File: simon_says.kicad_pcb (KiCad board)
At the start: 2 copper layers, 97 x 60 mm, 19 parts, among them SW1 SW_Push_LED, SW2 SW_Push_LED, SW3 SW_Push_LED, SW4 SW_Push_LED, U1 ATtiny25-20P

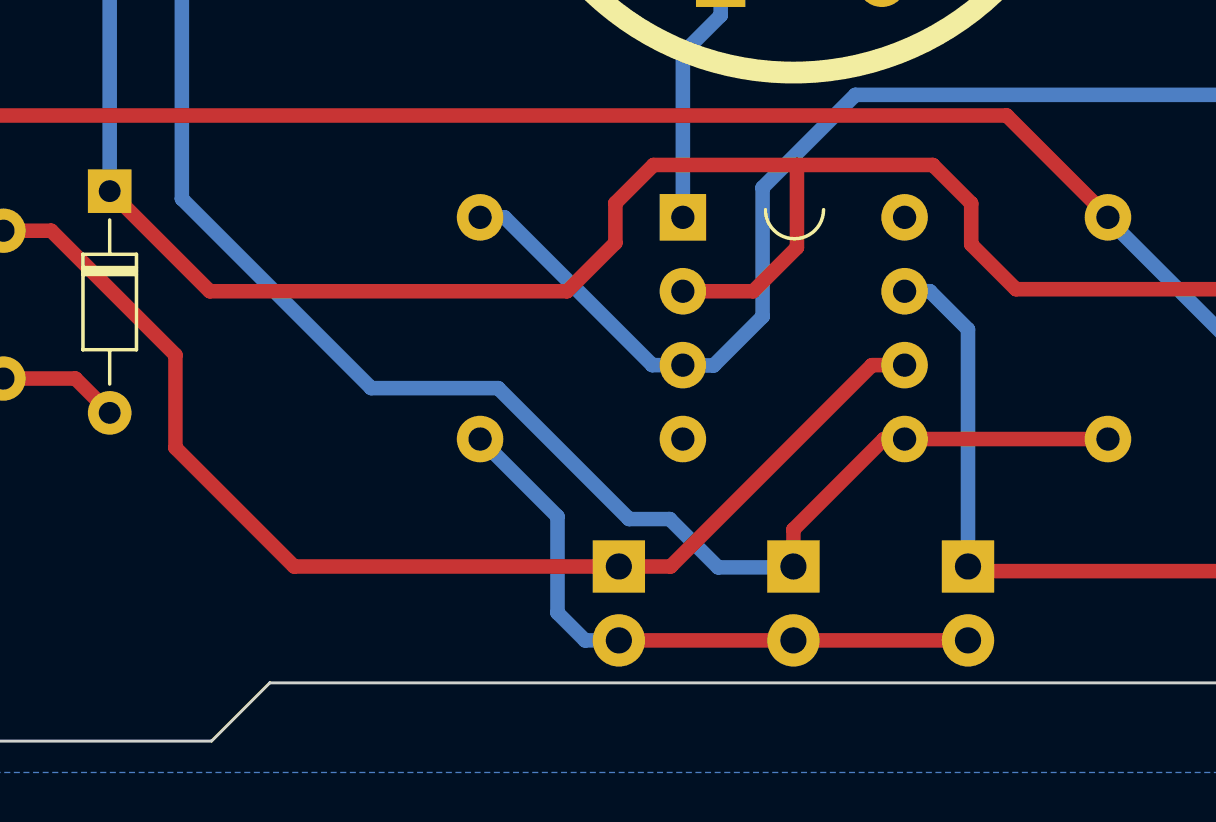
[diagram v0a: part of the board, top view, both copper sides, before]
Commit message: Added pads for power
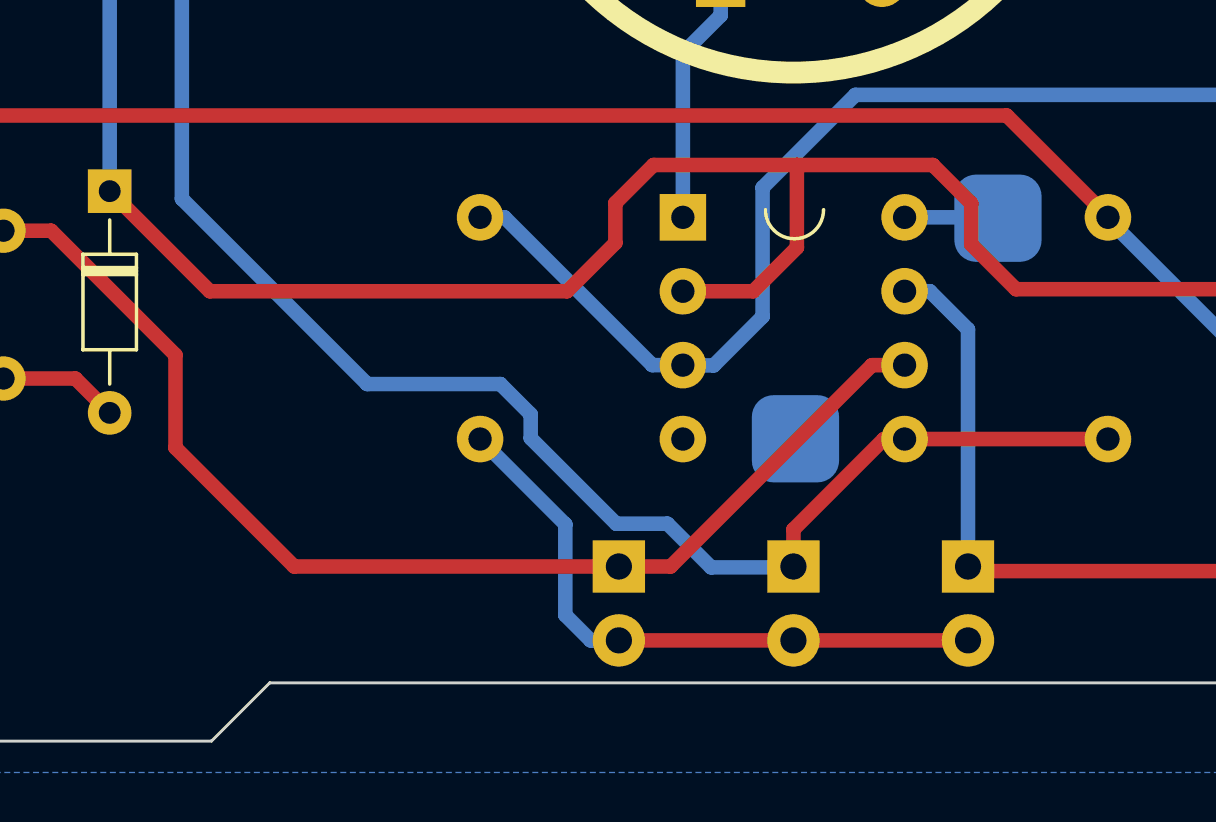
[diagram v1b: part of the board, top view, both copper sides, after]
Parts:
- added REF**: SolderWirePad_1x01_SMD_1x2mm, Connector_Wire:SolderWirePad_1x01_SMD_1x2mm, B.Cu at (98.6, 149.6)
- added REF**: SolderWirePad_1x01_SMD_1x2mm, Connector_Wire:SolderWirePad_1x01_SMD_1x2mm, B.Cu at (105.5, 142.0)
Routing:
- net +BATT: track 0.00 -> 3.44 mm
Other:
- board text added: "+"
- board text added: "-"
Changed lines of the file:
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@@
     (pad "1" thru_hole circle locked (at 0 0) (size 4.7 4.7) (drill 2.7) (layers "*.Cu" "*.Mask"))
   )
+  (footprint "Connector_Wire:SolderWirePad_1x01_SMD_1x2mm" (layer "B.Cu")
+    (at 98.57 149.61 180)
+    (descr "Wire Pad, Square, SMD Pad,  1mm x 2mm,")
+    (tags "MesurementPoint Square SMDPad 1mmx2mm ")
+    (attr exclude_from_pos_files exclude_from_bom)
+    (fp_text reference "REF**" (at 0 2.54) (layer "B.SilkS") hide
+        (effects (font (size 1 1) (thickness 0.15)) (justify mirror))
+    )
+    (fp_text value "SolderWirePad_1x01_SMD_1x2mm" (at 0 -2.54) (layer "B.Fab") hide
+        (effects (font (size 1 1) (thickness 0.15)) (justify mirror))
+    )
+    (pad "1" smd roundrect (at 0 0 180) (size 3 3) (layers "B.Cu" "B.Paste" "B.Mask") (roundrect_rratio 0.25)
+      (net 13 "-BATT"))
+  )
+  (footprint "Connector_Wire:SolderWirePad_1x01_SMD_1x2mm" (layer "B.Cu")
+    (at 105.53 142.03 180)
+    (descr "Wire Pad, Square, SMD Pad,  1mm x 2mm,")
+    (tags "MesurementPoint Square SMDPad 1mmx2mm ")
+    (attr exclude_from_pos_files exclude_from_bom)
+    (fp_text reference "REF**" (at 0 2.54) (layer "B.SilkS") hide
+        (effects (font (size 1 1) (thickness 0.15)) (justify mirror))
+    )
+    (fp_text value "SolderWirePad_1x01_SMD_1x2mm" (at 0 -2.54) (layer "B.Fab") hide
+        (effects (font (size 1 1) (thickness 0.15)) (justify mirror))
+    )
+    (pad "1" smd roundrect (at 0 0 180) (size 3 3) (layers "B.Cu" "B.Paste" "B.Mask") (roundrect_rratio 0.25)
+      (net 14 "+BATT"))
+  )
   (gr_line (start 115 103) (end 115 115.5)
     (stroke (width 0.32) (type default)) (layer "F.Cu"))
@@
     )
   )
+  (gr_text "+" (at 105.57 138.86) (layer "B.SilkS")
+    (effects (font (size 2 2) (thickness 0.3) bold) (justify mirror))
+  )
+  (gr_text "-" (at 99.63 147.7) (layer "B.SilkS")
+    (effects (font (size 1.5 1.5) (thickness 0.3) bold) (justify left bottom mirror))
+  )
   (segment (start 98.62 140.2) (end 103.29 140.2) (width 0.5) (layer "F.Cu") (net 1))
   (segment (start 104.61 141.52) (end 104.61 142.93) (width 0.5) (layer "F.Cu") (net 1))
@@
   (segment (start 102.32 149.62) (end 101.61 149.62) (width 0.5) (layer "F.Cu") (net 7))
   (segment (start 101.61 149.62) (end 98.5 152.73) (width 0.5) (layer "F.Cu") (net 7))
-  (segment (start 77.48 141.36) (end 83.99 147.87) (width 0.5) (layer "B.Cu") (net 7))
-  (segment (start 92.85 152.37) (end 94.25 152.37) (width 0.5) (layer "B.Cu") (net 7))
-  (segment (start 88.35 147.87) (end 92.85 152.37) (width 0.5) (layer "B.Cu") (net 7))
+  (segment (start 92.41 152.53) (end 94.17 152.53) (width 0.5) (layer "B.Cu") (net 7))
+  (segment (start 95.67 154.03) (end 98.47 154.03) (width 0.5) (layer "B.Cu") (net 7))
+  (segment (start 77.48 117.51) (end 77.48 141.36) (width 0.5) (layer "B.Cu") (net 7))
+  (segment (start 88.43 147.73) (end 89.47 148.77) (width 0.5) (layer "B.Cu") (net 7))
+  (segment (start 83.85 147.73) (end 88.43 147.73) (width 0.5) (layer "B.Cu") (net 7))
   (segment (start 72.63 116.27) (end 76.24 116.27) (width 0.5) (layer "B.Cu") (net 7))
   (segment (start 76.24 116.27) (end 77.48 117.51) (width 0.5) (layer "B.Cu") (net 7))
-  (segment (start 94.25 152.37) (end 95.91 154.03) (width 0.5) (layer "B.Cu") (net 7))
-  (segment (start 95.91 154.03) (end 98.47 154.03) (width 0.5) (layer "B.Cu") (net 7))
-  (segment (start 98.47 154.03) (end 98.5 154) (width 0.5) (layer "B.Cu") (net 7))
   (segment (start 71.35 117.54) (end 71.36 117.54) (width 0.5) (layer "B.Cu") (net 7))
-  (segment (start 77.48 117.51) (end 77.48 141.36) (width 0.5) (layer "B.Cu") (net 7))
+  (segment (start 89.47 149.59) (end 92.41 152.53) (width 0.5) (layer "B.Cu") (net 7))
   (segment (start 71.36 117.54) (end 72.63 116.27) (width 0.5) (layer "B.Cu") (net 7))
-  (segment (start 83.99 147.87) (end 88.35 147.87) (width 0.5) (layer "B.Cu") (net 7))
+  (segment (start 89.47 148.77) (end 89.47 149.59) (width 0.5) (layer "B.Cu") (net 7))
+  (segment (start 77.48 141.36) (end 83.85 147.73) (width 0.5) (layer "B.Cu") (net 7))
+  (segment (start 94.17 152.53) (end 95.67 154.03) (width 0.5) (layer "B.Cu") (net 7))
+  (segment (start 98.47 154.03) (end 98.5 154) (width 0.5) (layer "B.Cu") (net 7))
   (segment (start 104.34 156.54) (end 104.5 156.7) (width 0.5) (layer "F.Cu") (net 8))
   (segment (start 92.5 156.54) (end 104.34 156.54) (width 0.5) (layer "F.Cu") (net 8))
-  (segment (start 90.39 152.28) (end 90.39 155.59) (width 0.5) (layer "B.Cu") (net 8))
-  (segment (start 87.73 149.62) (end 90.39 152.28) (width 0.5) (layer "B.Cu") (net 8))
-  (segment (start 91.34 156.54) (end 92.5 156.54) (width 0.5) (layer "B.Cu") (net 8))
-  (segment (start 90.39 155.59) (end 91.34 156.54) (width 0.5) (layer "B.Cu") (net 8))
+  (segment (start 87.73 149.62) (end 90.66 152.55) (width 0.5) (layer "B.Cu") (net 8))
+  (segment (start 90.66 155.67) (end 91.53 156.54) (width 0.5) (layer "B.Cu") (net 8))
+  (segment (start 90.66 152.55) (end 90.66 155.67) (width 0.5) (layer "B.Cu") (net 8))
+  (segment (start 91.53 156.54) (end 92.5 156.54) (width 0.5) (layer "B.Cu") (net 8))
   (segment (start 94.28 154) (end 81.34 154) (width 0.5) (layer "F.Cu") (net 9))
   (segment (start 77.26 146.73) (end 72.99 142.46) (width 0.5) (layer "F.Cu") (net 9))
@@
   (segment (start 96 133.92) (end 96 135.06) (width 0.5) (layer "B.Cu") (net 12))
   (segment (start 96 135.06) (end 94.7 136.36) (width 0.5) (layer "B.Cu") (net 12))
+  (segment (start 102.32 142) (end 105.58 142) (width 0.5) (layer "B.Cu") (net 14))
+  (segment (start 105.58 142) (end 105.71 141.87) (width 0.25) (layer "B.Cu") (net 14))
   (zone (net 13) (net_name "-BATT") (layer "B.Cu") (hatch edge 0.5)
     (connect_pads (clearance 0.5))

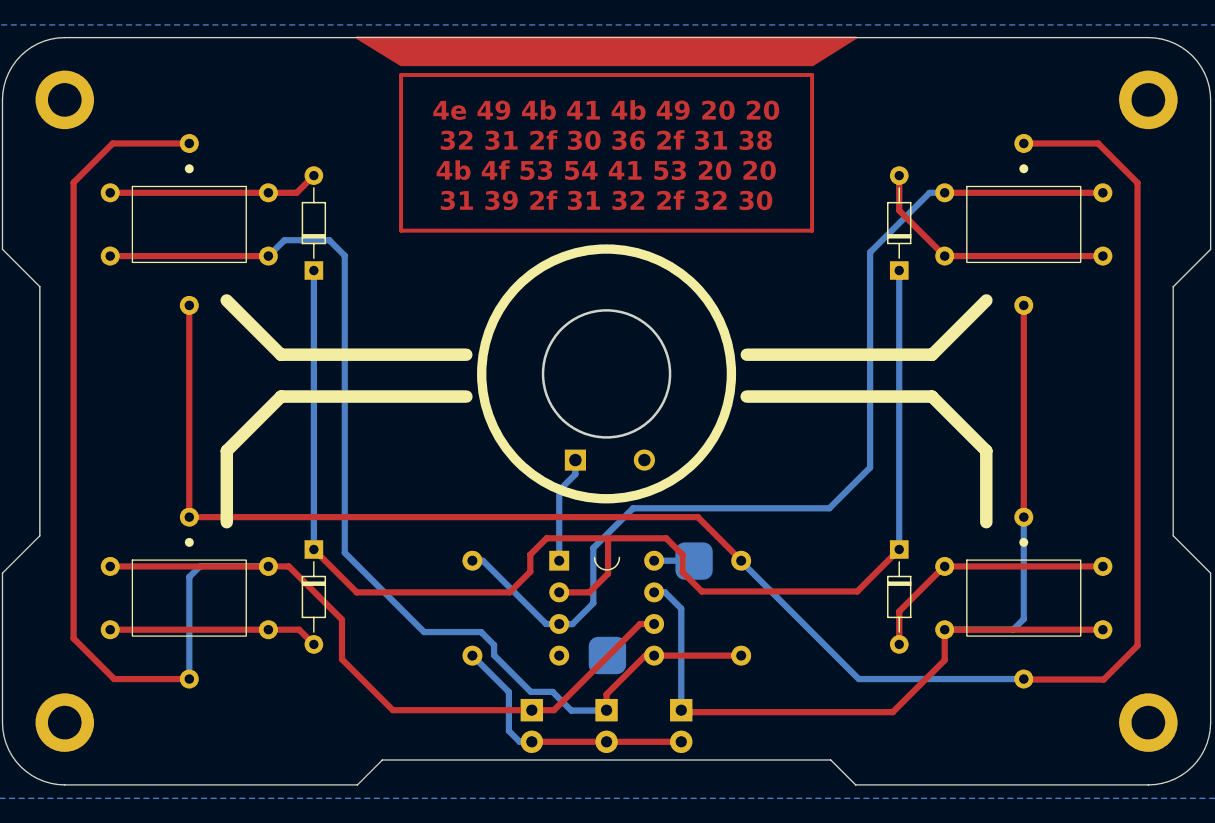
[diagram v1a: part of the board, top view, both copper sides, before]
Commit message: Added CR battery pads and removed redundant LEDs
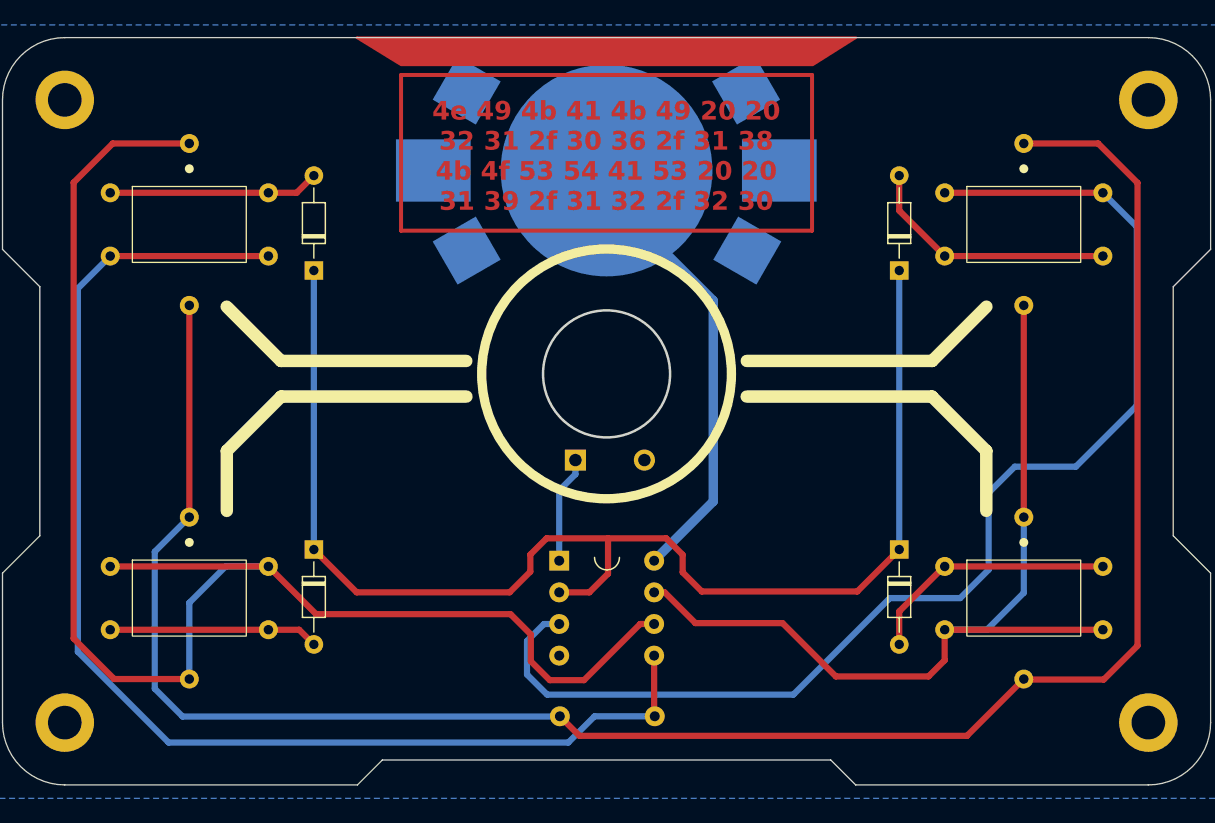
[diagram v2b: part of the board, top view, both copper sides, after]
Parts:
- removed D10, D6, D8: LED, LED_THT:LED_D1.8mm_W3.3mm_H2.4mm
- removed R2: 50R, Resistor_THT:R_Axial_DIN0207_L6.3mm_D2.5mm_P7.62mm_Horizontal
- added ?: , , F.Cu at (88.8, 104.3)
- added ?: , , F.Cu at (87.4, 117.1)
- added ?: , , F.Cu at (85.6, 110.7)
- added ?: , , F.Cu at (111.4, 104.3)
- added REF**: SolderWirePad_1x01_SMD_1x2mm, Connector_Wire:SolderWirePad_1x01_SMD_1x2mm, B.Cu at (109.7, 117.1)
- moved REF** 41.1 mm to (111.9, 110.7), turned to -90 degrees
- moved REF** 32.1 mm to (98.5, 110.7)
- moved R1 8.48 mm to (102.4, 154.5), turned to 180 degrees
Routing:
- net +BATT: track 3.44 -> 36.8 mm
- net Net-(D10-A): track 21.5 -> 0.00 mm
- net MM4: track 79.9 -> 99.7 mm
- net MM1: track 83.8 -> 100.7 mm
- net Net-(SW1-A): track 147.3 -> 163.1 mm
- net MM3: track 80.9 -> 72.5 mm
- net MM2: track 125.9 -> 122.1 mm
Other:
- board text added: "CR2450"
- board text removed: "+"
- board text removed: "-"

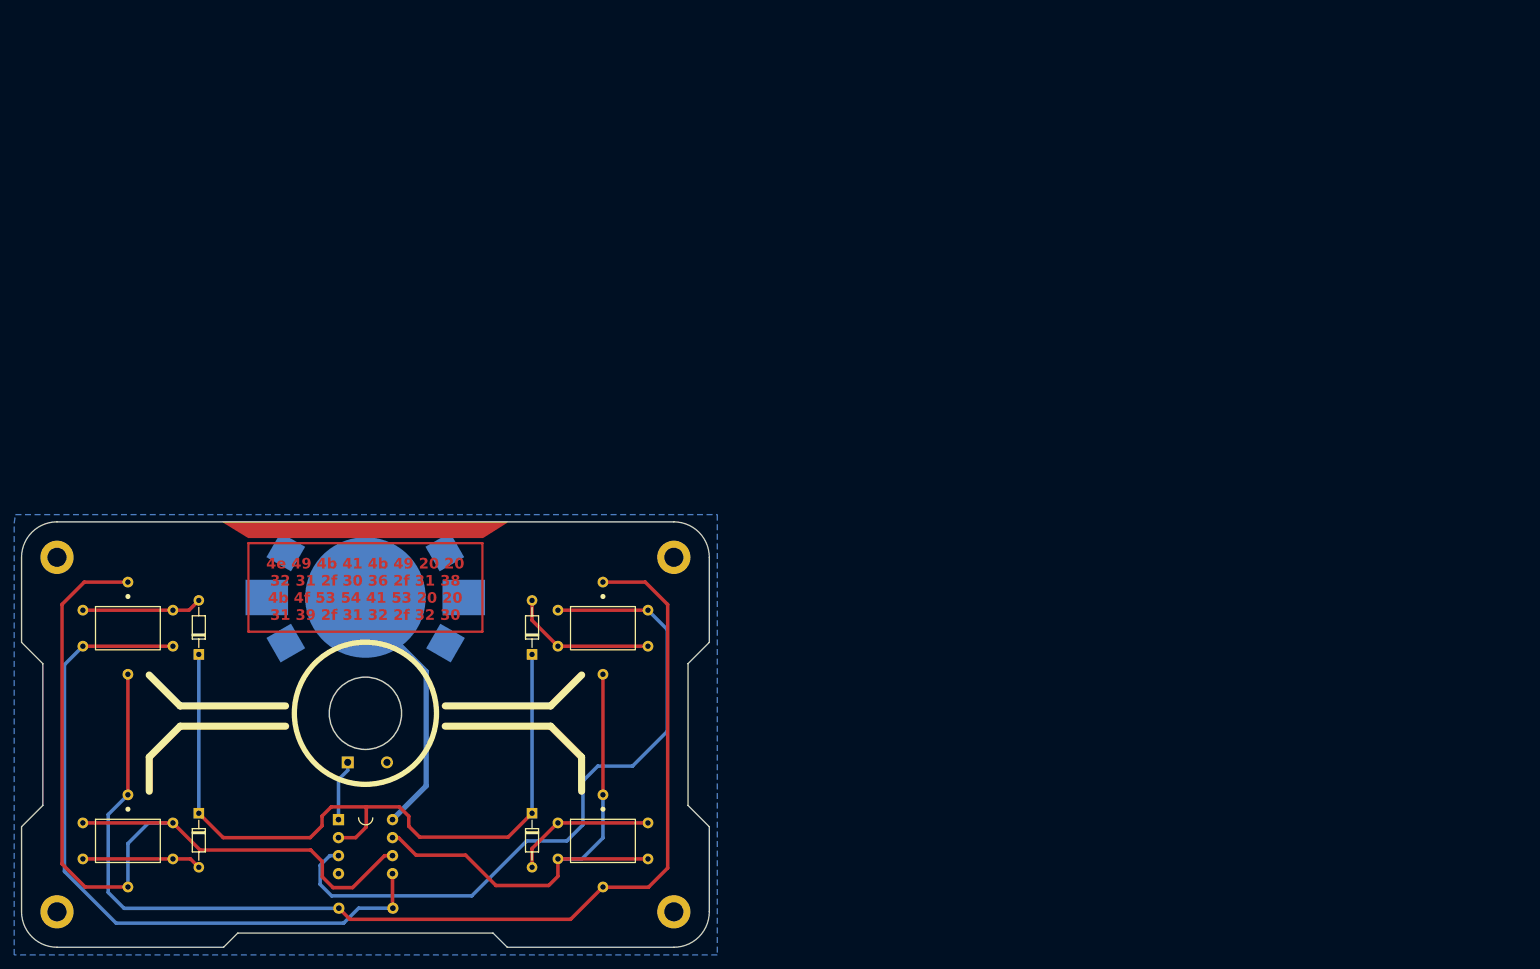
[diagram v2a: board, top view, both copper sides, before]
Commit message: Updated front face decorations
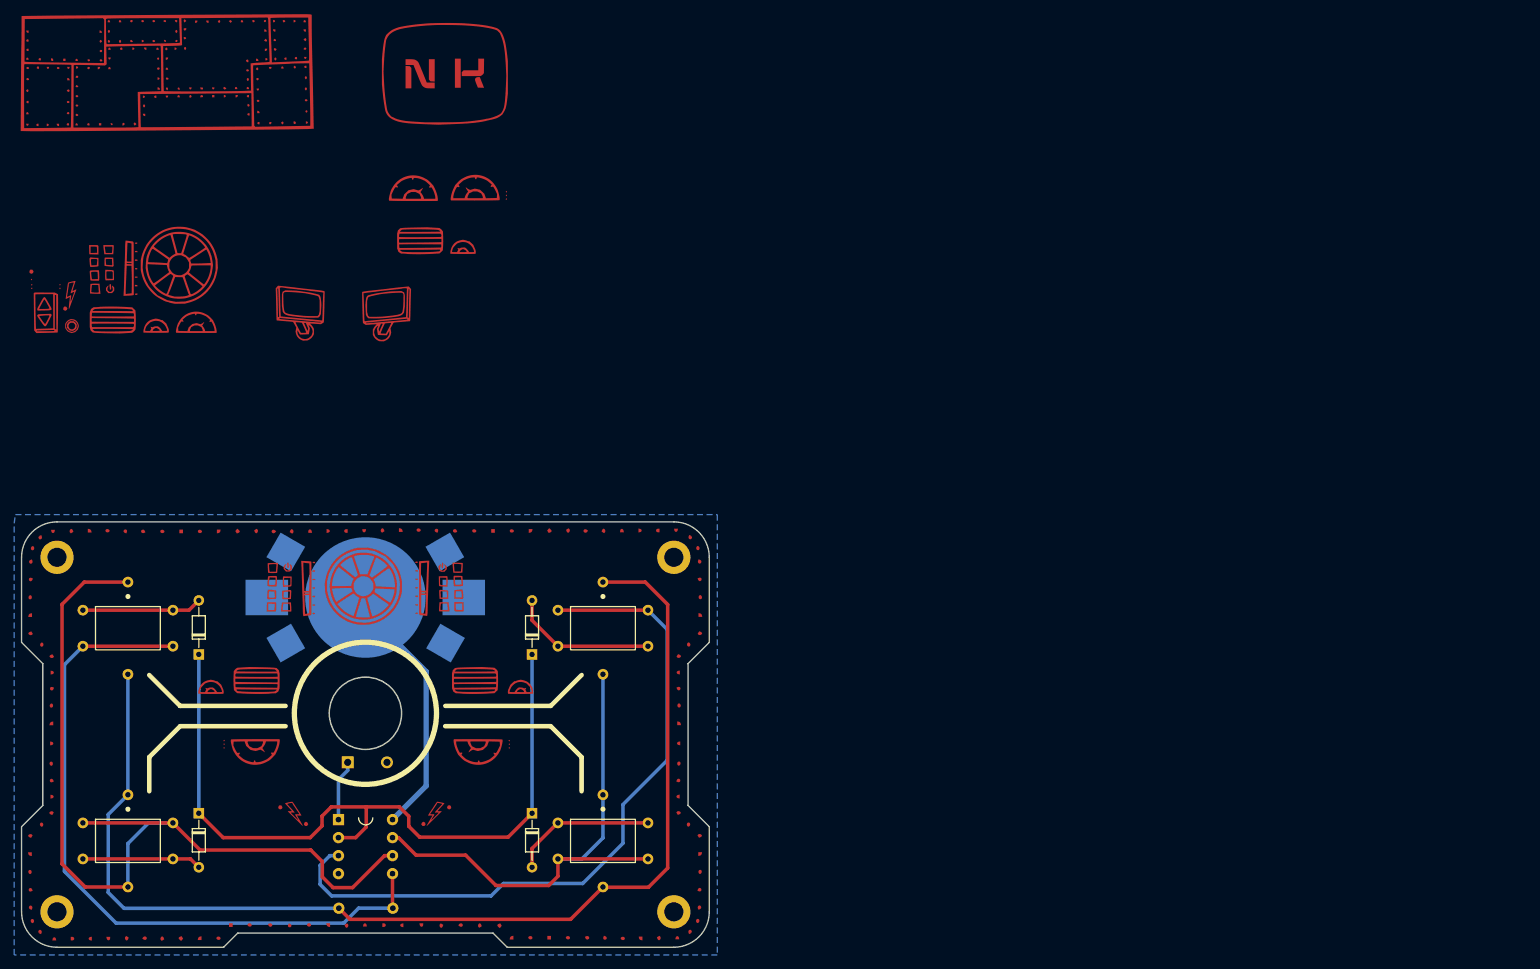
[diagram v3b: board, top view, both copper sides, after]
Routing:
- net MM4: track 99.7 -> 101.7 mm
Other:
- board text removed: "4e 49 4b 41 4b 49 20 20 32 31 2f 30 36 2f 31 38 4b 4f 53 54 41 53 20 20 31 39 2f 31 32 2f 32 30"
